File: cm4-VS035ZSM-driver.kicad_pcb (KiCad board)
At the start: 4 copper layers, 38 x 40 mm, 89 parts, among them J301 245863050104829+, J302 Conn_01x22, J304 Conn_01x04_power_jumpers, J305 Conn_01x03_Pin, U202 TPS65132WRVCR_C2876379, U203 LP3320B6F, U204 MCP1603T-180I/OS

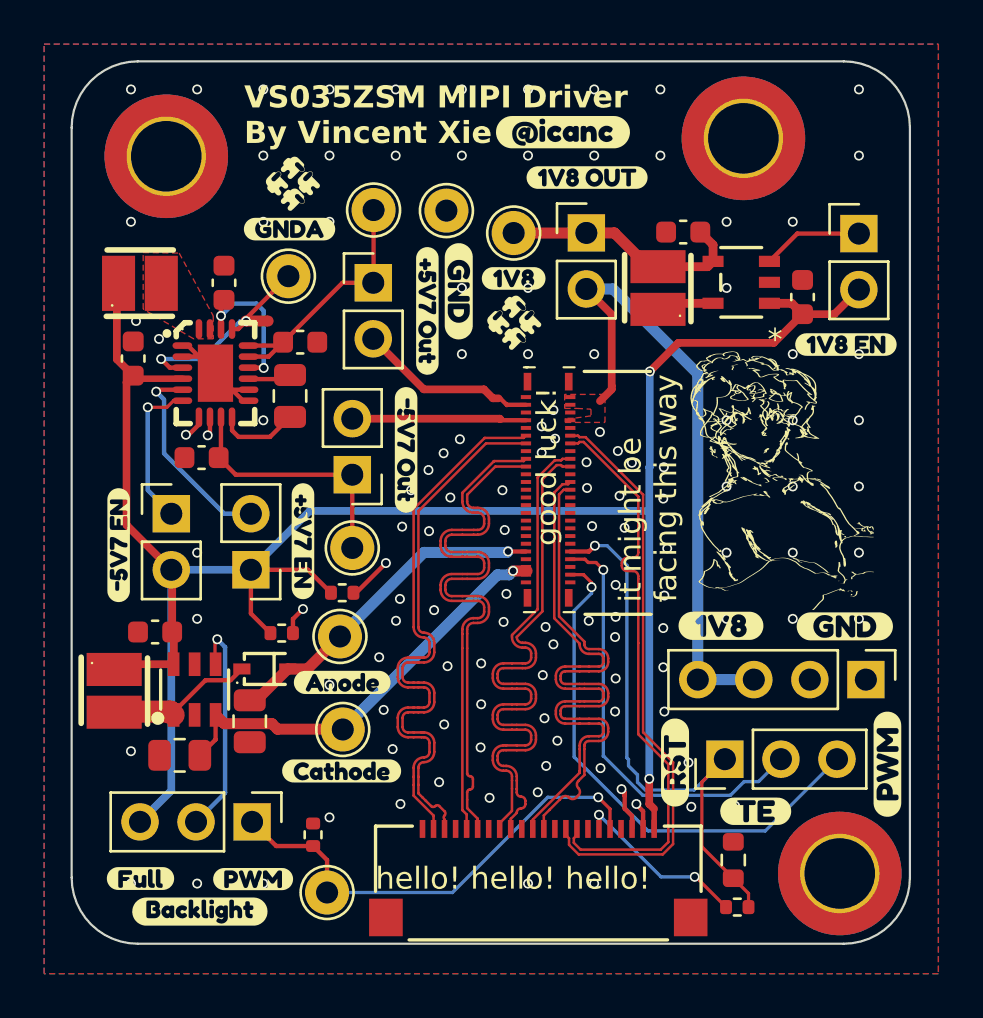
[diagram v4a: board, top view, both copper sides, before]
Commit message: better driver design now that the cm5 has pin swapping support
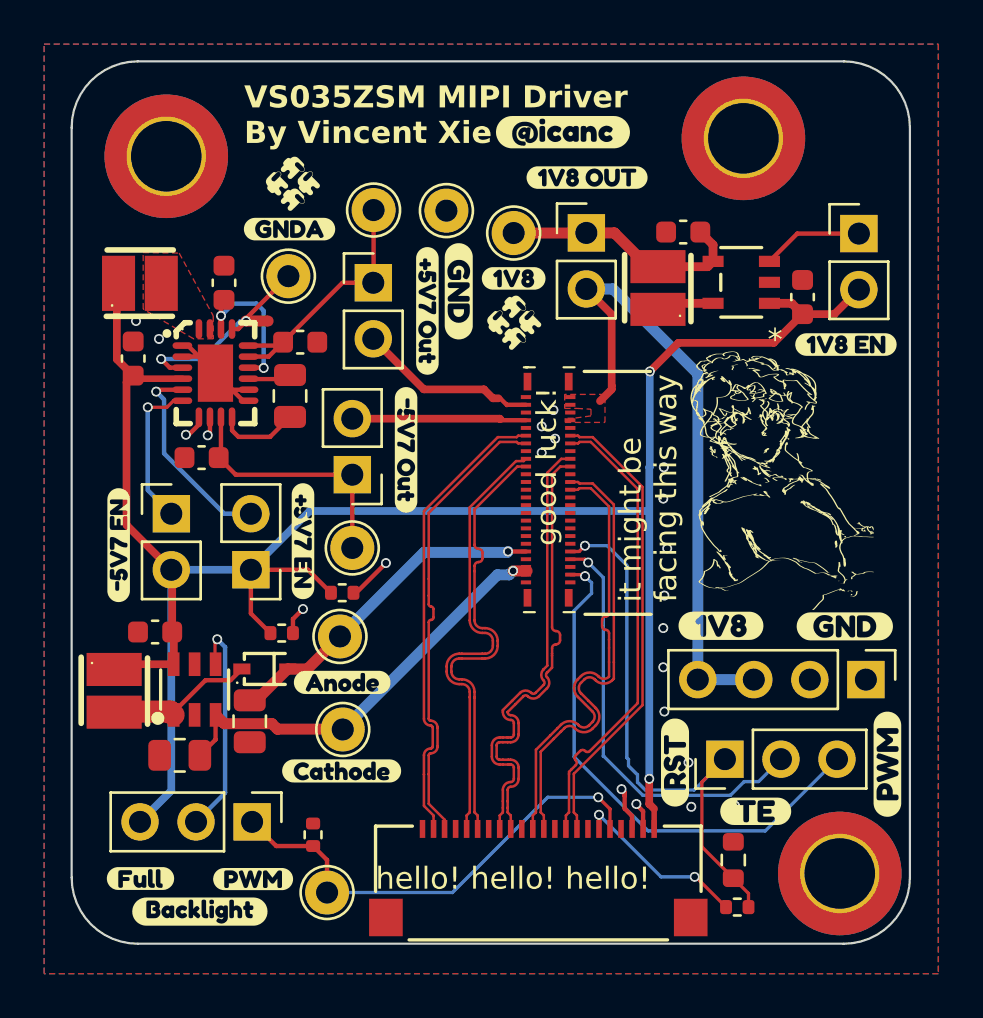
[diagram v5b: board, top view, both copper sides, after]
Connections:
- J302 pad 11: /high-speed/DSI0_DATA.2_N -> /high-speed/DSI0_DATA.2_P
- J302 pad 12: /high-speed/DSI0_DATA.2_P -> /high-speed/DSI0_DATA.2_N
- J302 pad 14: /high-speed/DSI0_DATA.3_N -> /high-speed/DSI0_DATA.3_P
- J302 pad 15: /high-speed/DSI0_DATA.3_P -> /high-speed/DSI0_DATA.3_N
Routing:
- net /high-speed/DSI0_DATA.3_N: track 26.7 -> 21.1 mm
- net /high-speed/DSI0_DATA.3_P: track 26.6 -> 21.1 mm
- net /high-speed/DSI0_DATA.2_N: track 26.5 -> 21.0 mm
- net /high-speed/DSI0_DATA.2_P: track 26.5 -> 20.9 mm
- net /high-speed/DSI0_CLK.N: track 26.5 -> 20.9 mm
- net /high-speed/DSI0_DATA.1_P: track 26.5 -> 21.0 mm
- net /high-speed/DSI0_CLK.P: track 26.4 -> 20.9 mm
- net /high-speed/DSI0_DATA.1_N: track 26.5 -> 21.0 mm
- net /high-speed/DSI0_DATA.0_N: track 26.5 -> 21.1 mm
- net /high-speed/DSI0_DATA.0_P: track 26.5 -> 21.0 mm
- net GND: vias 117 -> 16

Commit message: ok imma try kicad 10
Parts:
- removed H305, H307, H308: MountingHole_Pad, MountingHole:MountingHole_3.2mm_M3_DIN965_Pad_TopBottom
- removed J301: 245863050104829+, footprints:245863050104829_missing pads
- removed J302: Conn_01x22, footprints:CON22_1X22_DRB_XF2C_TYC
- removed J304: Conn_01x04_power_jumpers, Connector_PinHeader_2.54mm:PinHeader_1x04_P2.54mm_Vertical
- removed J305: Conn_01x03_Pin, Connector_PinHeader_2.54mm:PinHeader_1x03_P2.54mm_Vertical
- removed JP203: 1.8-bridge, Connector_PinHeader_2.54mm:PinHeader_1x02_P2.54mm_Vertical
- removed JP204: Enable-1V8, Connector_PinHeader_2.54mm:PinHeader_1x02_P2.54mm_Vertical
- removed JP205: Backlight_Jumper, Connector_PinHeader_2.54mm:PinHeader_1x03_P2.54mm_Vertical
- removed JP208: +5.7_bridge, Connector_PinHeader_2.54mm:PinHeader_1x02_P2.54mm_Vertical
- removed JP209: -5v7_bridge, Connector_PinHeader_2.54mm:PinHeader_1x02_P2.54mm_Vertical
- removed JP210: Jumper+, Connector_PinHeader_2.54mm:PinHeader_1x02_P2.54mm_Vertical
- removed JP211: Jumper-, Connector_PinHeader_2.54mm:PinHeader_1x02_P2.54mm_Vertical
- removed NT201: NetTie_GND, NetTie:NetTie-2_SMD_Pad0.5mm
- removed R301, R302, R303: 2.2kΩ, Resistor_SMD:R_0402_1005Metric
- removed R304: 2.7kΩ, Resistor_SMD:R_0603_1608Metric
- removed TP203: TestPoint_GND_PAD, TestPoint:TestPoint_THTPad_D2.0mm_Drill1.0mm
- removed TP204: TestPoint_GNDA_PAD, TestPoint:TestPoint_THTPad_D2.0mm_Drill1.0mm
- removed TP205: TestPoint_anode, TestPoint:TestPoint_THTPad_D2.0mm_Drill1.0mm
- removed TP206: TestPoint_cathode, TestPoint:TestPoint_THTPad_D2.0mm_Drill1.0mm
- removed TP207: TestPoint_PWM, TestPoint:TestPoint_THTPad_D2.0mm_Drill1.0mm
- removed TP208: TestPoint_P_5V7, TestPoint:TestPoint_THTPad_D2.0mm_Drill1.0mm
- removed TP209: TestPoint_N_5V7, TestPoint:TestPoint_THTPad_D2.0mm_Drill1.0mm
- added H1: MountingHole_Pad, MountingHole:MountingHole_3.2mm_M3_DIN965_Pad_TopBottom, F.Cu at (181.2, 6.66)
- added H2: MountingHole_Pad, MountingHole:MountingHole_3.2mm_M3_DIN965_Pad_TopBottom, F.Cu at (181.2, 13.8)
- added H3: MountingHole_Pad, MountingHole:MountingHole_3.2mm_M3_DIN965_Pad_TopBottom, F.Cu at (181.2, 21.0)
- added J1: Conn_01x22, footprints:CON22_1X22_DRB_XF2C_TYC, F.Cu at (194.6, 30.5)
- added J3: 245863050104829+, footprints:245863050104829_missing pads, F.Cu at (191.3, 51.0)
- added R3: 2.2kΩ, Resistor_SMD:R_0402_1005Metric, F.Cu at (173.2, 57.3)
- added R4: 2.7kΩ, Resistor_SMD:R_0603_1608Metric, F.Cu at (175.2, 57.5)
- added U1: PZ254-2-08-WS, footprints:HDR-SMD_16P-P2.54-H-M-R2-C8-W12.0-N, F.Cu at (218.2, 42.5)
- added U2: KF1027B-04P-G00-DFT-01B, footprints:SW-SMD_KF1027B-04P-G00-DFT-01B, F.Cu at (222.7, 65.3)
- added U3: KF1027B-04P-G00-DFT-01B, footprints:SW-SMD_KF1027B-04P-G00-DFT-01B, F.Cu at (199.1, 65.2)
- added kibuzzard-6996886F: G***, kibuzzard-6996886F, F.Cu at (191.6, 65.3)
- moved R209 89.6 mm to (179.6, -21.2), turned to -90 degrees
- moved C216 83.7 mm to (178.2, -24.7), turned to 180 degrees
- moved R206 82.0 mm to (180.2, -17.4), turned to -90 degrees
- moved L204 81.7 mm to (173.3, -19.9)
- moved U203 81.5 mm to (177.0, -19.7)
- moved C221 78.4 mm to (211.8, -27.8), turned to 90 degrees
- moved L207 78.3 mm to (205.0, -30.2)
- moved C222 78.3 mm to (209.3, -30.0), turned to 0 degrees
- moved U202 78.2 mm to (208.5, -26.0)
- moved C223 78.1 mm to (205.1, -26.5)
- moved C220 78.0 mm to (208.7, -21.6), turned to -90 degrees
- moved D403 77.1 mm to (176.2, -16.1), turned to -90 degrees
- moved C215 76.8 mm to (177.4, -13.5), turned to 0 degrees
- moved C213 76.3 mm to (213.8, -22.2)
- moved kibuzzard-685CA5ED 63.2 mm to (130.2, 93.4)
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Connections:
- net +3V3 renamed +5V_IN
- net /MIPI-screen/LED_PWR.A renamed /LED_PWR.A_OUT
- net /MIPI-screen/LED_PWR.K renamed /LED_PWR.K
- net /MIPI-screen/OUTN renamed /-5V7_OUT
- net /MIPI-screen/OUTP renamed /+5V7_OUT
- net /MIPI-screen/SW renamed /SW
- net Net-(JP203-A) renamed /1V8_OUT
- U202 pad 17: GNDA -> GND
- U202 pad 3: GNDA -> GND
- U202 pad 5: Net-(JP208-B) -> /+5V7_EN
- U202 pad 6: Net-(JP209-A) -> /-5V7_EN
- U202 pad 7: SCL_3V3 -> SDA_3V3
- U202 pad 8: SDA_3V3 -> SCL_3V3
- U203 pad 4: /MIPI-screen/BACKLIGHT_EN -> LED_PWM
- U204 pad 3: Net-(JP204-A) -> /1V8_EN
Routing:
- net +5V_IN: track 98.4 -> 0.00 mm, vias 2 -> 0
- net SCL_3V3: track 33.8 -> 0.00 mm, vias 3 -> 0
- net /DSI0_CLK.N: track 0.00 -> 32.3 mm
- net SDA_3V3: track 32.2 -> 0.00 mm, vias 3 -> 0
- net /DSI0_CLK.P: track 0.00 -> 30.5 mm
- net +1V8: track 28.8 -> 0.00 mm
- net /DSI0_DATA.3_N: track 0.00 -> 25.9 mm
- net LCD_RESET_DISPLAY_SIDE: track 25.8 -> 0.00 mm, vias 1 -> 0
- net /DSI0_DATA.3_P: track 0.00 -> 25.5 mm
- net /DSI0_DATA.0_N: track 0.00 -> 24.3 mm
- net LCD_CONNECTOR_PWM: track 24.0 -> 0.00 mm, vias 1 -> 0
- net /DSI0_DATA.0_P: track 0.00 -> 24.0 mm
- net /DSI0_DATA.2_N: track 0.00 -> 22.3 mm
- net /DSI0_DATA.2_P: track 0.00 -> 21.9 mm
- net /DSI0_DATA.1_N: track 0.00 -> 21.8 mm
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- added copper zone on F.Cu, net (none)
- removed copper zone on F.Cu, net +1V8
- removed copper zone on F.Cu, net /SW
- removed copper zone on B.Cu, net GND
- removed copper zone on F.Cu, net GND
- removed copper zone on In1.Cu, net GND
- removed copper zone on In2.Cu, net GND
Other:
- board size 38 x 40 mm -> 50 x 50 mm

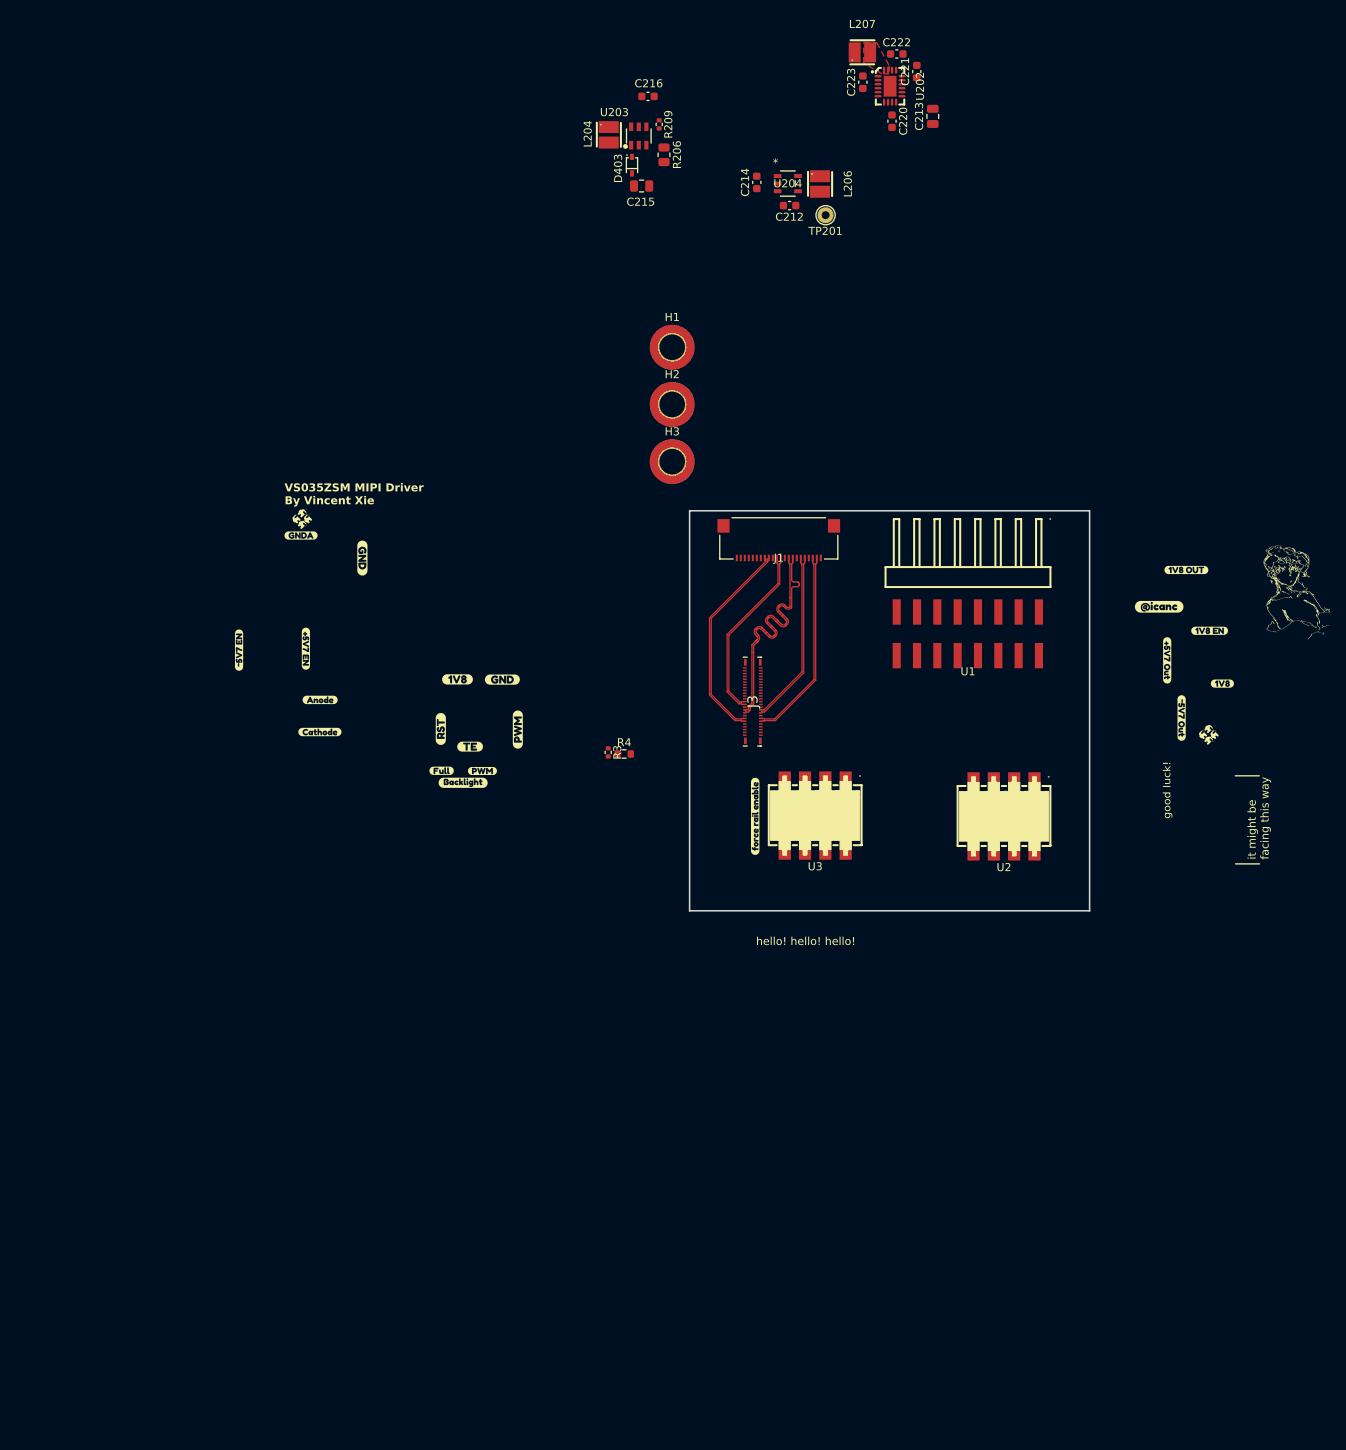
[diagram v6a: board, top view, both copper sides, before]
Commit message: finalized board before rounding corners
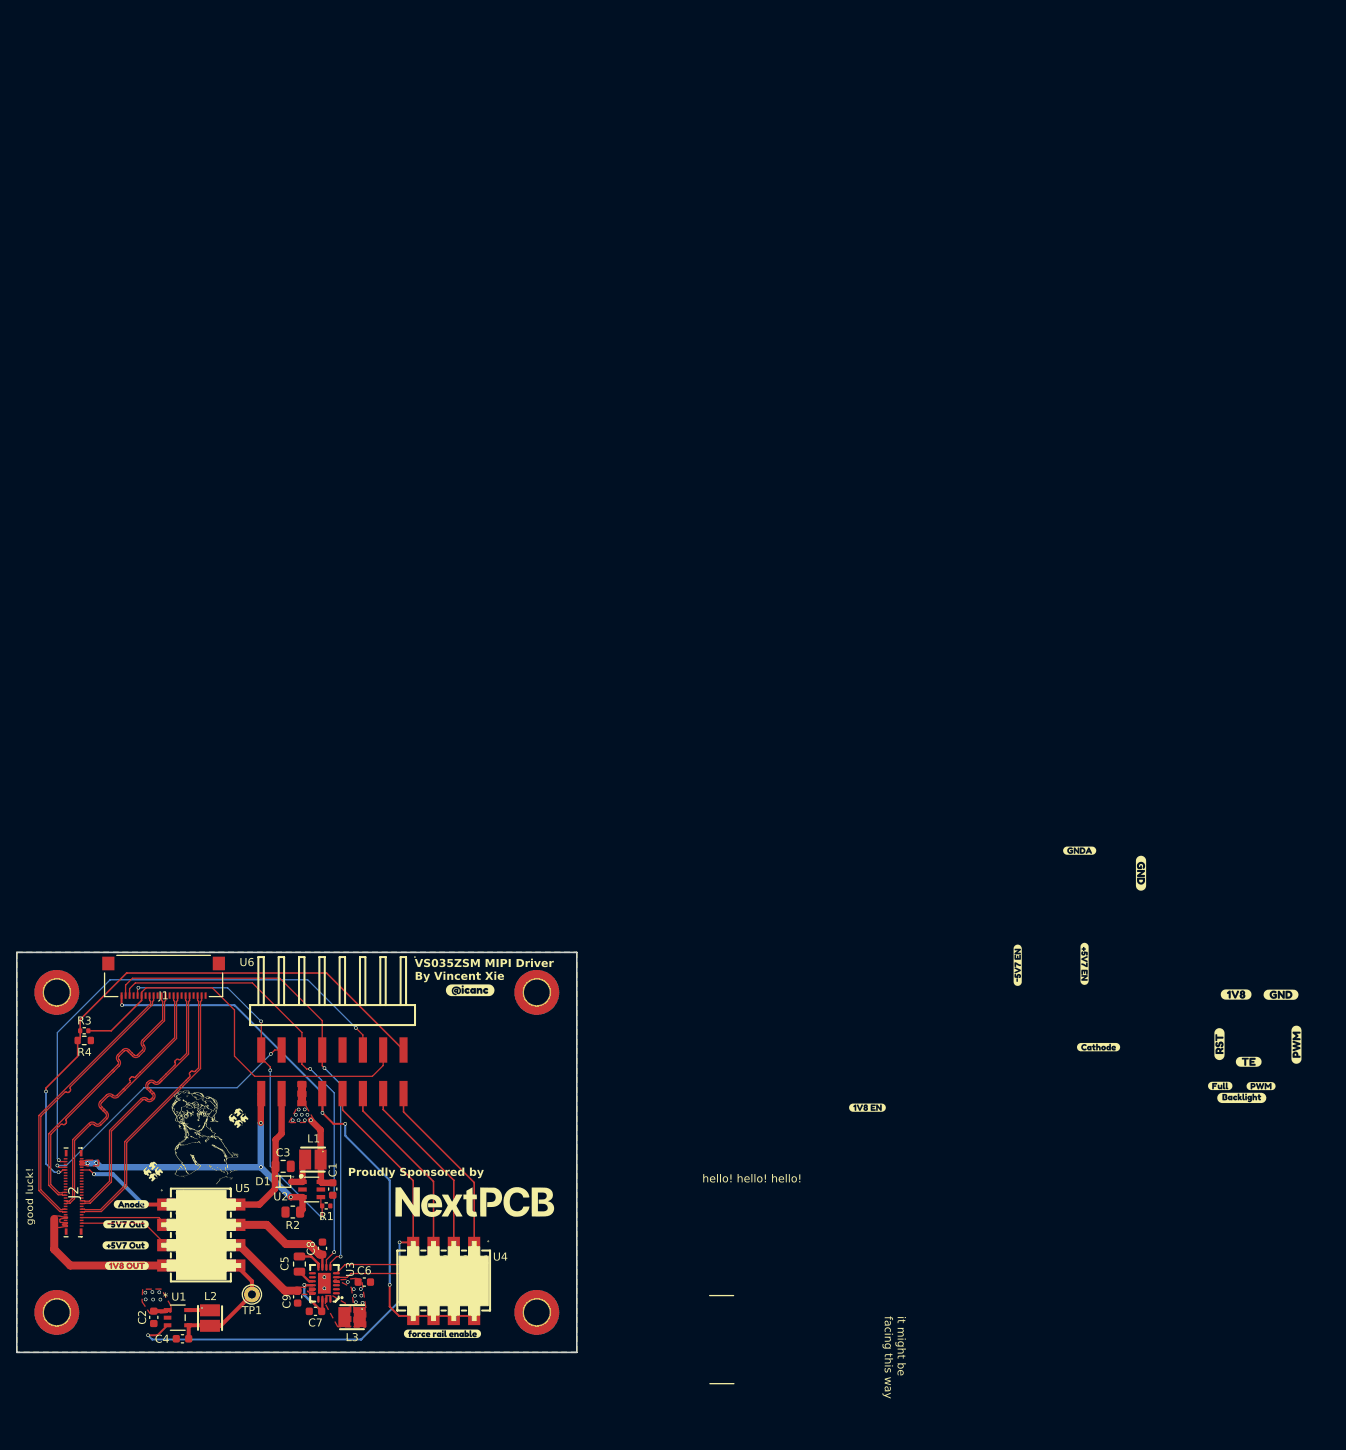
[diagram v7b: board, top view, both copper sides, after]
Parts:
- removed the kibuzzard-685CA70B at (250.0, 48.7)
- added G***: LOGO, LOGO, F.Cu at (153.7, 114.3)
- added H3: MountingHole_Pad, MountingHole:MountingHole_3.2mm_M3_DIN965_Pad_TopBottom, F.Cu at (164.3, 127.3)
- moved C7 173.2 mm to (136.6, 127.2), turned to 180 degrees
- moved C9 171.6 mm to (134.4, 125.4), turned to -90 degrees
- moved L3 170.5 mm to (141.2, 127.9), turned to 180 degrees
- moved U3 165.5 mm to (137.8, 123.7), turned to 90 degrees
- moved C5 163.9 mm to (134.6, 121.3), turned to -90 degrees
- moved C6 162.4 mm to (142.7, 123.5), turned to 0 degrees
- moved L2 161.0 mm to (123.4, 128.0)
- moved U1 161.0 mm to (119.4, 128.0)
- moved C4 160.7 mm to (120.0, 130.6)
- moved C2 160.7 mm to (116.4, 127.9)
- moved kibuzzard-685CA724 158.4 mm to (113.1, 121.5)
- moved C8 157.9 mm to (137.5, 119.3), turned to 90 degrees
- moved TP1 152.8 mm to (128.7, 125.1)
- moved G*** 152.5 mm to (120.2, 101.1)
- moved kibuzzard-685CA6D3 149.3 mm to (112.9, 118.9), turned to 0 degrees
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- renumbered C216 to C1, C214 to C2, C215 to C3, C212 to C4, C213 to C5, C223 to C6, C222 to C7, C220 to C8, C221 to C9, D403 to D1, H3 to H4, J3 to J2, L204 to L1, L206 to L2, L207 to L3, R209 to R1, R206 to R2, TP201 to TP1, U204 to U1, U203 to U2, U202 to U3, U2 to U4, U3 to U5, U1 to U6
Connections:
- J1 pad 17: LCD_RESET -> LCD_RESET_3V3
- U6 pad 11: TE -> SCL_3V3
- U6 pad 13: SCL_3V3 -> TE
- U6 pad 15: SDA_3V3 -> LED_PWM
- U6 pad 7: LCD_RESET -> unconnected-(U6-Pad7)
- U6 pad 9: LED_PWM -> SDA_3V3
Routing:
- net +3V3: track 0.00 -> 75.3 mm, vias 0 -> 4
- net LCD_RESET_1V8: track 0.00 -> 69.6 mm, vias 0 -> 2
- net /1V8_EN: track 0.00 -> 68.5 mm, vias 0 -> 2
- net LCD_CONNECTOR_PWM: track 0.00 -> 62.6 mm, vias 0 -> 2
- net SDA_3V3: track 0.00 -> 61.0 mm, vias 0 -> 2
- net SCL_3V3: track 0.00 -> 57.0 mm, vias 0 -> 2
- net LCD_RESET_3V3: track 0.00 -> 50.1 mm
- net LED_PWM: track 0.00 -> 48.6 mm, vias 0 -> 4
- net /LED_PWR.K: track 0.00 -> 39.9 mm, vias 0 -> 5
- net /-5V7_EN: track 0.00 -> 39.6 mm, vias 0 -> 2
- net /+5V7_EN: track 0.00 -> 37.6 mm
- net TE: track 0.00 -> 35.1 mm, vias 0 -> 2
- net /BL_DRV_EN: track 0.00 -> 22.7 mm
- net +1V8: track 0.00 -> 18.7 mm
- net /LED_PWR.A_OUT: track 0.00 -> 17.9 mm
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- added copper zone on F.Cu, net +1V8
- added copper zone on F.Cu, net +5V_IN
- added copper zone on In2.Cu, net +5V_IN
- added copper zone on F.Cu, net /+5V7_OUT
- added copper zone on F.Cu, net /LED_PWR.K
- added copper zone on F.Cu, net /SW
- added copper zone on B.Cu, net GND
- added copper zone on F.Cu, net GND
- added copper zone on In1.Cu, net GND
- added copper zone on In2.Cu, net GND
- removed copper zone on F.Cu, net (none)
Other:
- board size 50 x 50 mm -> 70 x 50 mm
- board text added: "Proudly Sponsored by"
- board text added: "stackup: Huaqiu04161H02-1080"
